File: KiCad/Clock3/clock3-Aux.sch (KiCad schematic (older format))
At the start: 49 parts, among them J1 V_IN, K1 PWR SEL, P10 CONN_1, P11 CONN_1, P12 V_OUT, P13 ISP Header, P14 CONN_1, P15 CONN_1, P16 CONN_1, P17 CONN_1, P18 CONN_1, P19 CONN_1, P20 CONN_1, P21 CONN_1, P22 CONN_1, P23 CONN_1, P24 DIL6, P25 DIL6, P26 DIL6, P27 DIL6, P28 DIL6, P29 DIL6, P30 DIL6, P31 DIL6, P32 DIL6, P33 DIL6, P34 DIL6, P35 DIL6, P36 DIL6, P37 DIL6, P38 DIL6, P39 DIL6, P41 STACK-L, P42 STACK-R, P48 7SegDisp, P7 FTDI, P8 CONN_1, P9 CONN_1, U5 7805

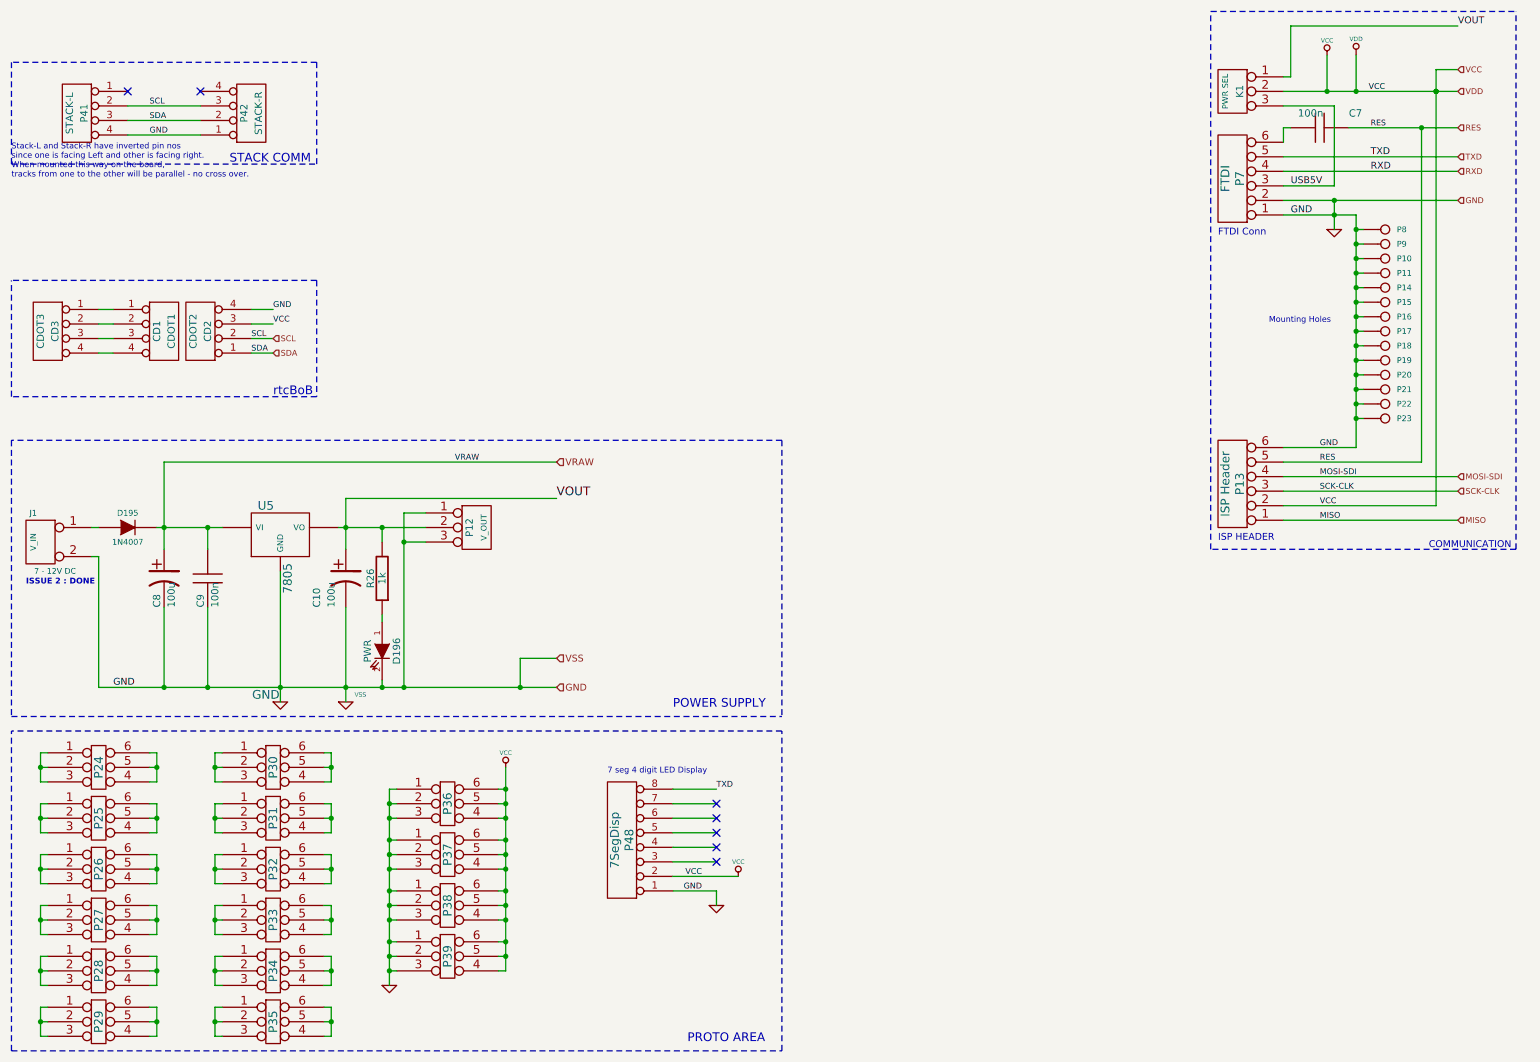
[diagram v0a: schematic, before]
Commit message: 
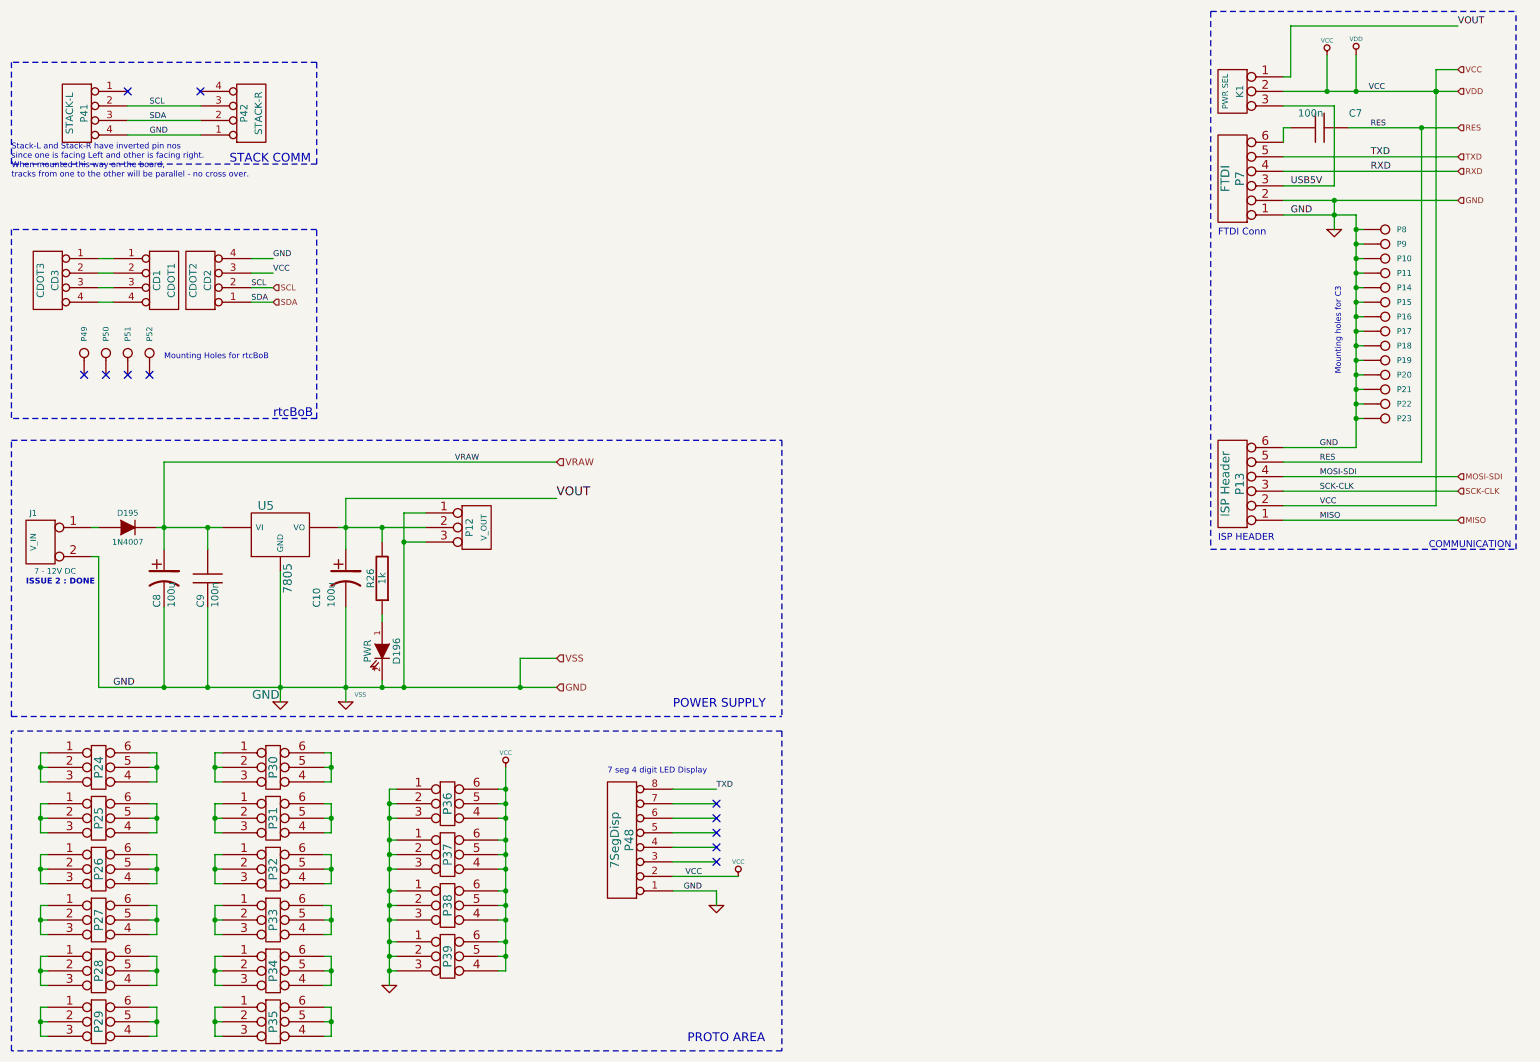
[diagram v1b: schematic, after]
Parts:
- added P49, P50, P51, P52: CONN_1, vite_3mm, symbol CONN_1
- C10, C8: footprint (none) -> CP_5x11mm
- C7, C9: footprint (none) -> C2
- CD1, CD2, CD3: footprint (none) -> pin_strip_4
- D195: footprint (none) -> diode_do41
- D196: footprint (none) -> led_5mm_clear
- J1: footprint (none) -> JACK_ALIM
- K1, P12: footprint (none) -> pin_strip_3
- P10, P11, P14, P15, P16, P17, P18, P19, P20, P21, P22, P23, P8, P9: footprint (none) -> vite_3mm
- P13: footprint (none) -> PIN_STRIP_3X2
- P24, P25, P26, P27, P28, P29, P30, P31, P32, P33, P34, P35, P36, P37, P38, P39: footprint (none) -> PROTO-6
- P41, P42: footprint (none) -> PIN_STRIP_4-90
- P48: footprint (none) -> pin_strip_8
- P7: footprint (none) -> PIN_STRIP_6-90
- R26: footprint (none) -> RC03
- U5: footprint (none) -> Volt_Reg_78xx
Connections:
- no-connect marks 7 -> 11
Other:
- note added: "Mounting Holes for rtcBoB"
- note added: "Mounting holes for C3"
- note removed: "Mounting Holes"
- moved on the sheet: CD1, CD2, CD3

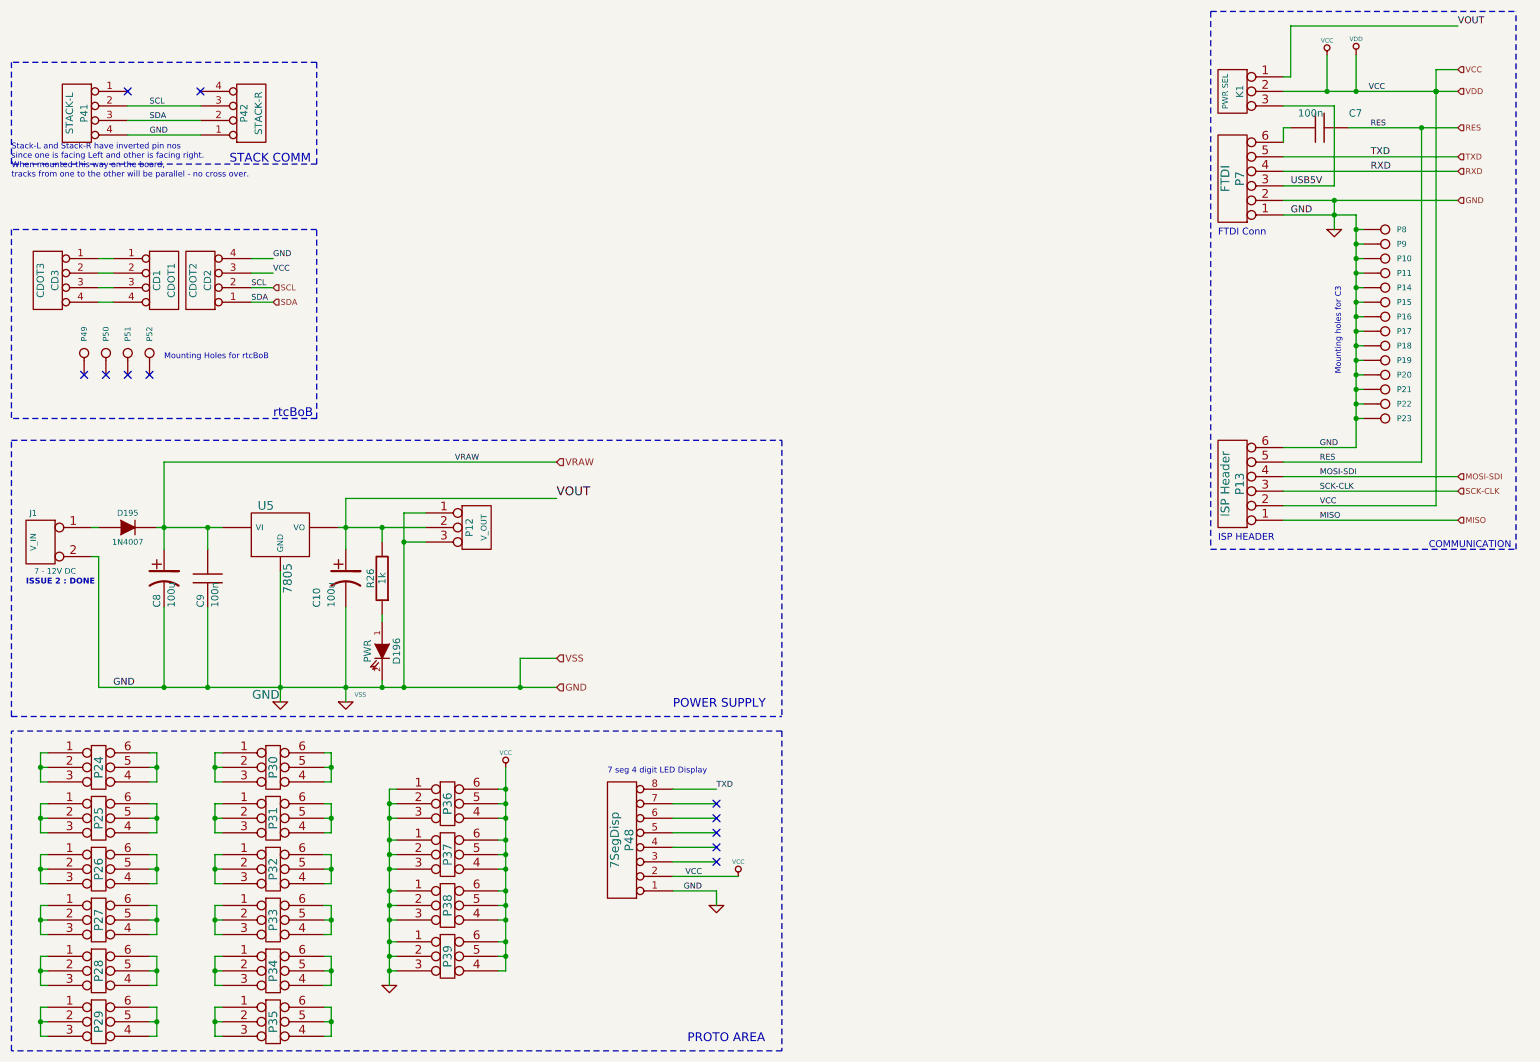
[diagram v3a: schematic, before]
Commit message: C3 Board Track layout changes , Legend, Clearances for Baffle
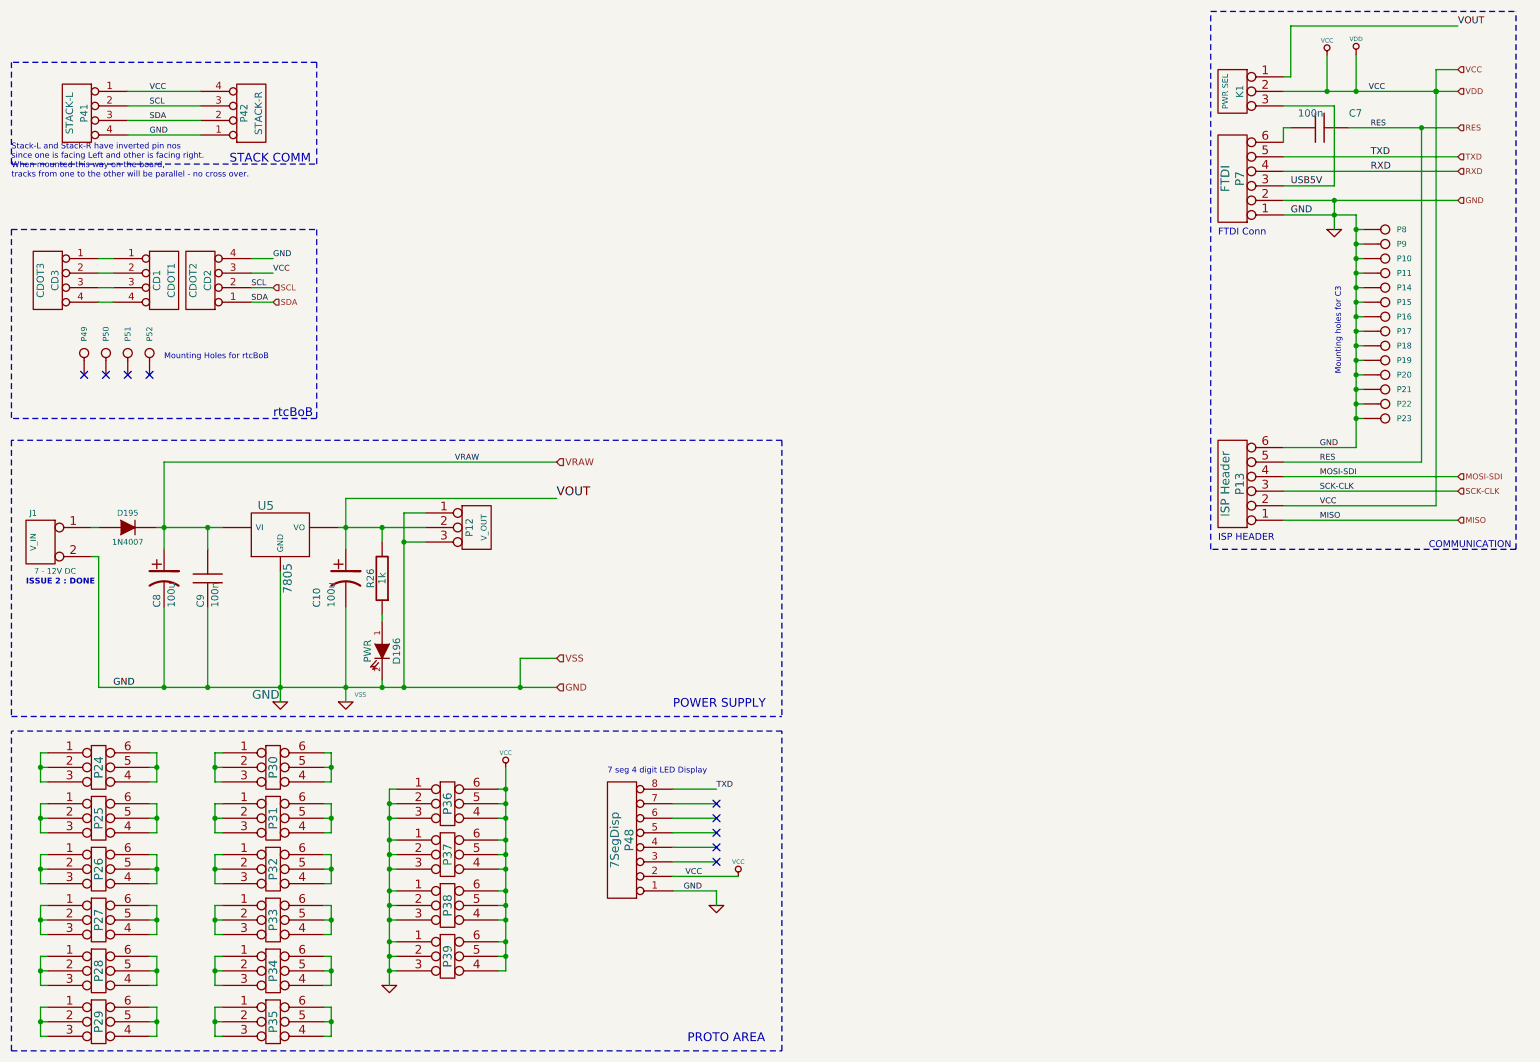
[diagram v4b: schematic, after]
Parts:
- D196: footprint led_5mm_clear -> led_5mm_blue
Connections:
- net VCC: now also P41.1 (P1), P42.4 (P4)
- no-connect marks 11 -> 9

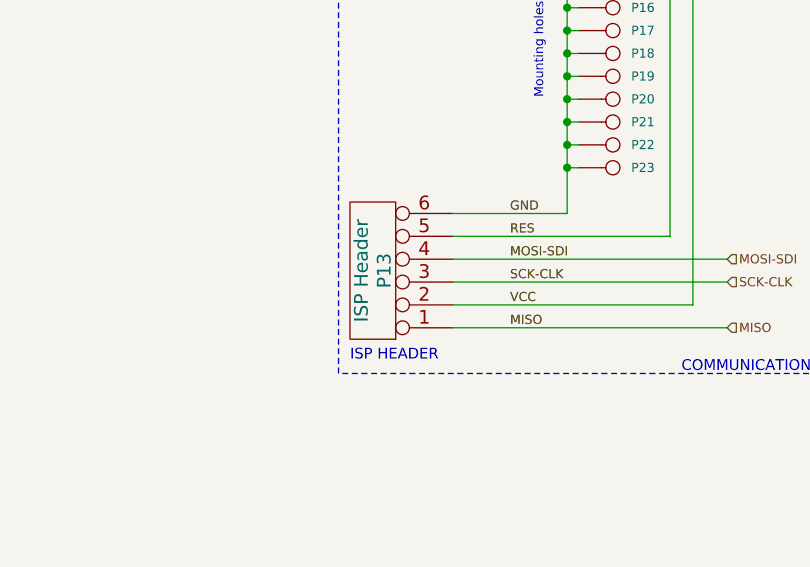
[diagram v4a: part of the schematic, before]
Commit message: C3 board layout - clearances for Baffle, rowBoB mounting etc
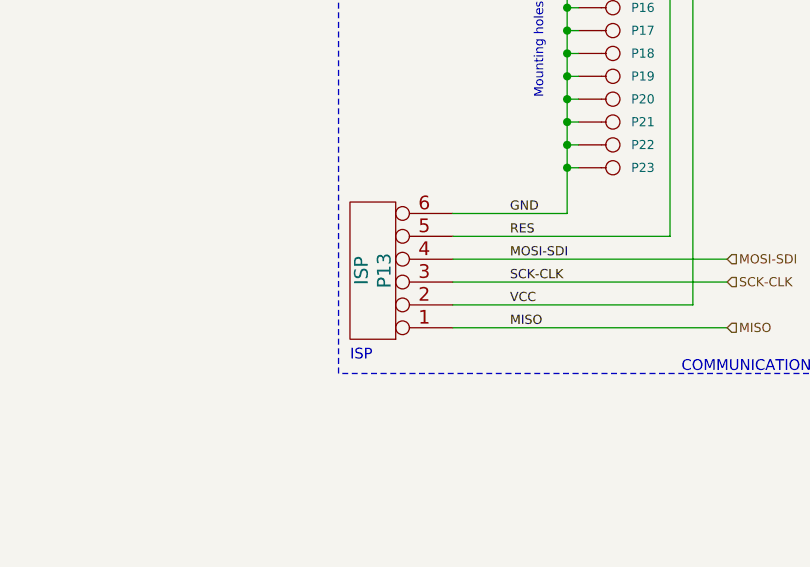
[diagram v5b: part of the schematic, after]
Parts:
- P13: value ISP Header -> ISP
- P41: footprint PIN_STRIP_4-90 -> pin_sck_4-90
- U5: footprint Volt_Reg_78xx -> VOLT_REG_78XX
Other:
- note added: "ISP"
- note removed: "ISP HEADER"
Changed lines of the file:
@@
-EESchema Schematic File Version 2  date 01/03/11 18:27:14
+EESchema Schematic File Version 2  date 01/04/11 18:15:53
 LIBS:clock3
 LIBS:power
@@
 Sheet 3 3
 Title "ClockTWO"
-Date "3 jan 2011"
+Date "4 jan 2011"
 Rev "A"
 Comp "wyojustin@gmail.com :: anool.m@gmail.com"
@@
 F 0 "P41" V 1150 1250 50  0000 C CNN
 F 1 "STACK-L" V 1250 1250 50  0000 C CNN
-F 2 "PIN_STRIP_4-90" H 1200 1250 60  0001 C CNN
+F 2 "pin_sck_4-90" H 1200 1250 60  0001 C CNN
 	1    1200 1250
 	-1   0    0    -1
@@
 VCC
 Text Notes 9050 4200 0    47   ~ 0
-ISP HEADER
+ISP
 Text Label 9750 3750 0    40   ~ 0
 MOSI-SDI
@@
 P 9150 3800
 F 0 "P13" V 9100 3800 60  0000 C CNN
-F 1 "ISP Header" V 9200 3800 60  0000 C CNN
+F 1 "ISP" V 9200 3800 60  0000 C CNN
 F 2 "PIN_STRIP_3X2" H 9150 3800 60  0001 C CNN
 	1    9150 3800
@@
 F 0 "U5" H 2500 4350 60  0000 C CNN
 F 1 "7805" V 2650 3850 60  0000 C CNN
-F 2 "Volt_Reg_78xx" H 2600 4150 60  0001 C CNN
+F 2 "VOLT_REG_78XX" H 2600 4150 60  0001 C CNN
 	1    2600 4150
 	1    0    0    -1
